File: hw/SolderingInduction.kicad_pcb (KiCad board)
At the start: 4 copper layers, 68.9 x 37.6 mm, 55 parts, among them J1 C116159, J3 RBP_GPIO_CONN, SW1 SW_Push, SW2 SW_Push, SW3 SW_Push, SW4 SW_Push, SW5 SW_Push, SW6 SW_Push, SW7 SW_Push, SW8 SW_Push, U1 ASM1117-3.3, U3 WQ25JVS, U4 RP2040, Y1 X322512MMB4SI

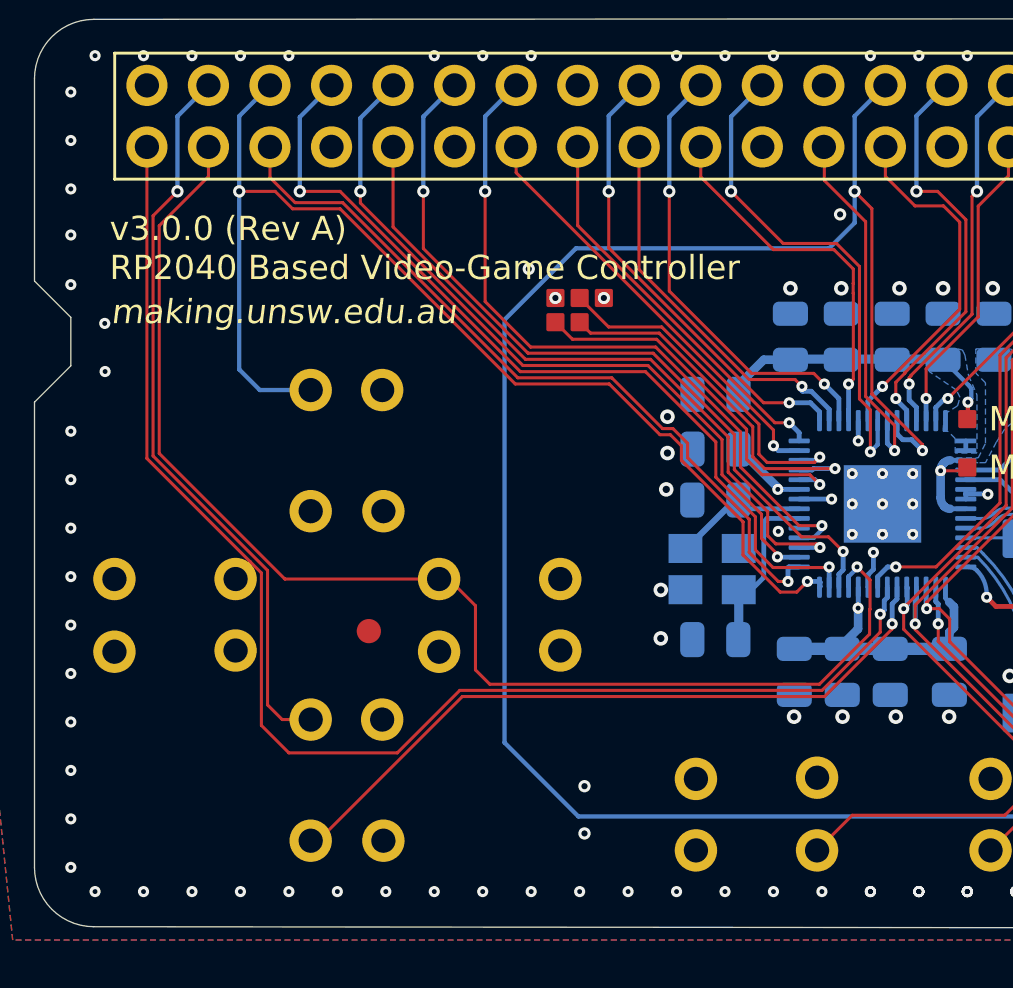
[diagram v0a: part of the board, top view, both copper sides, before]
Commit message: Merge conflict, resolved w/ fw
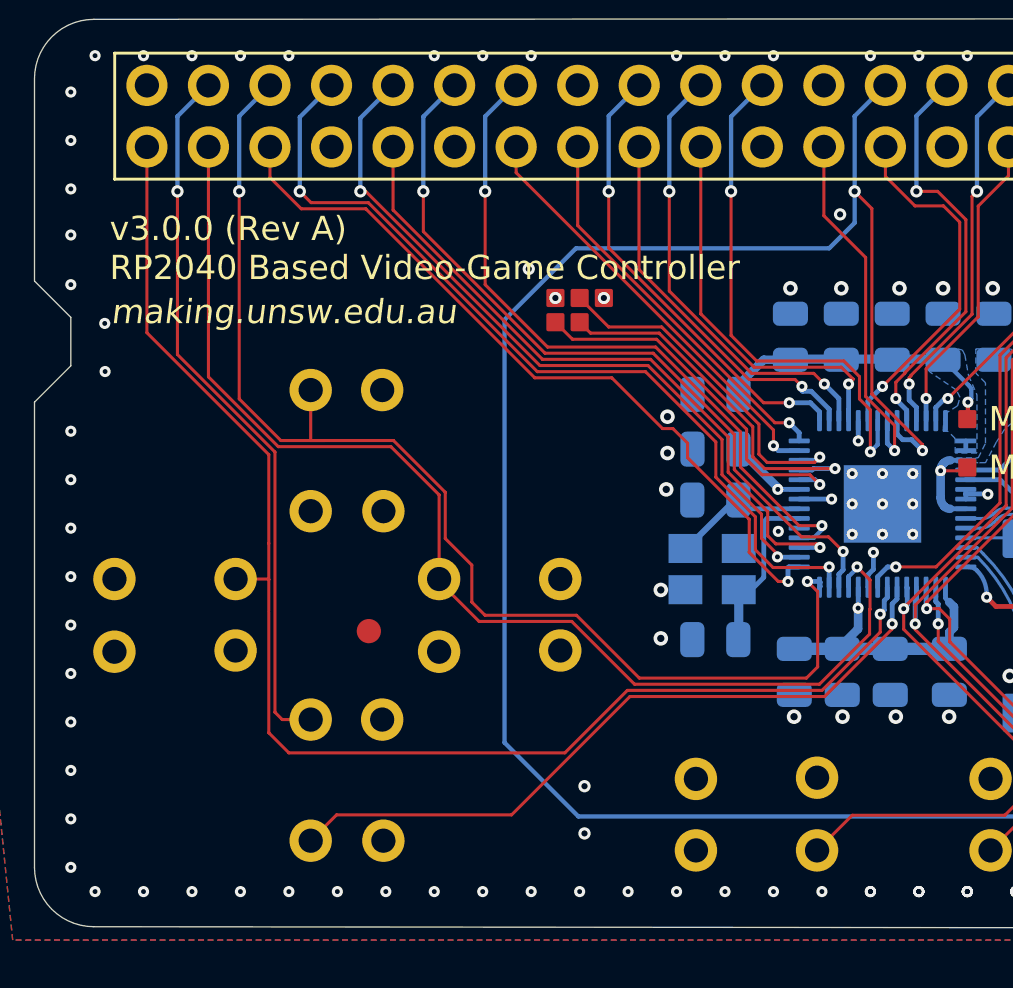
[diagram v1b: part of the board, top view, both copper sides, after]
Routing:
- net /$.GPIO8: track 53.5 -> 49.3 mm
- net /$.GPIO11: track 47.9 -> 51.4 mm
- net /$.GPIO4: track 59.9 -> 59.1 mm
- net /$.GPIO23: track 20.7 -> 21.6 mm
- net /$.GPIO21: track 15.5 -> 16.1 mm

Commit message: Repo cleanup
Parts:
- moved R5 0.56 mm to (148.9, 64.2)
- moved R1 0.17 mm to (154.3, 64.2)
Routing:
- net /USB_VBUS: track 13.1 -> 17.3 mm
- net /$.GPIO5: track 57.3 -> 59.9 mm
- net /$.GPIO11: track 51.4 -> 49.3 mm
- net /$.GPIO8: track 49.3 -> 48.0 mm
- net /$.GPIO10: track 35.7 -> 34.8 mm
- net /$.GPIO9: track 31.8 -> 30.9 mm
- net /$.GPIO14: track 28.3 -> 27.4 mm
- net /$.GPIO15: track 28.9 -> 28.0 mm
- net /$.GPIO13: track 30.8 -> 29.9 mm
- net GND: vias 145 -> 146

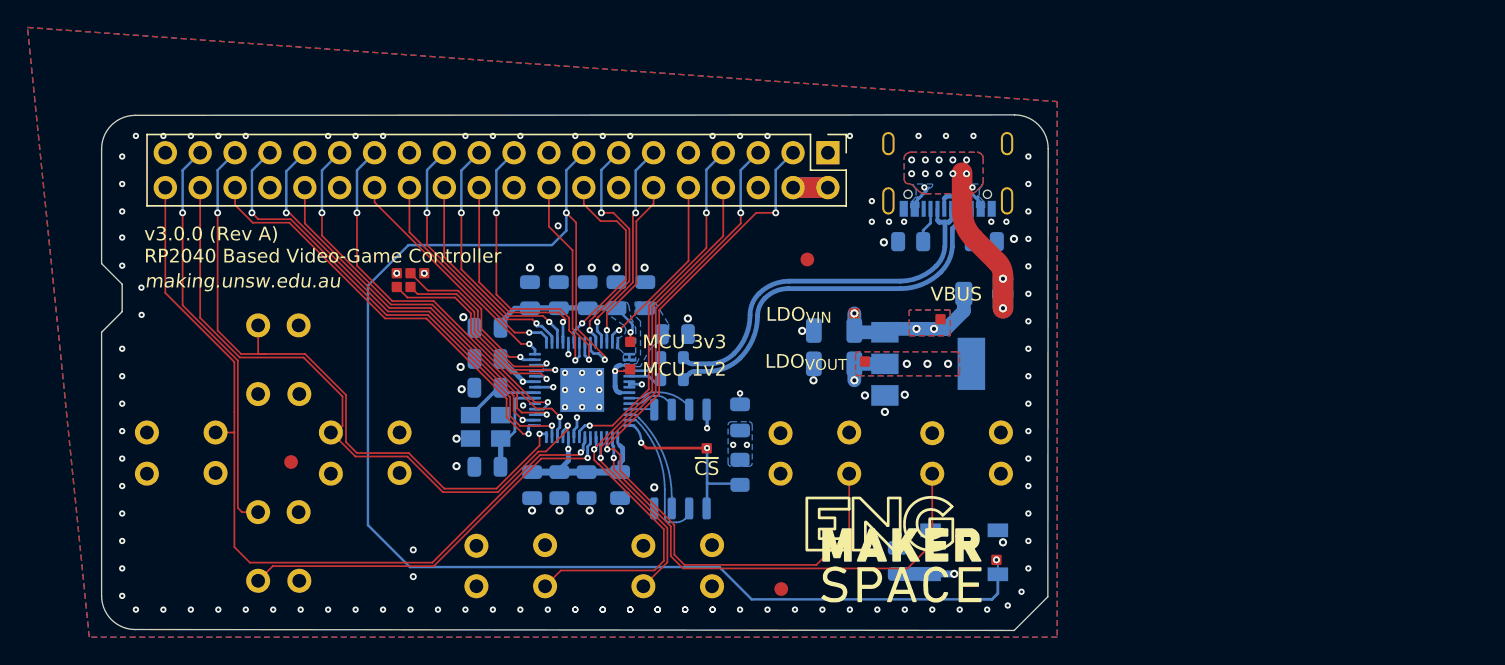
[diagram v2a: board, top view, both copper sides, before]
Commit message: v4.0.0 hw version begins here. Cleaning pinmaps, LED line, power layout, USB layout
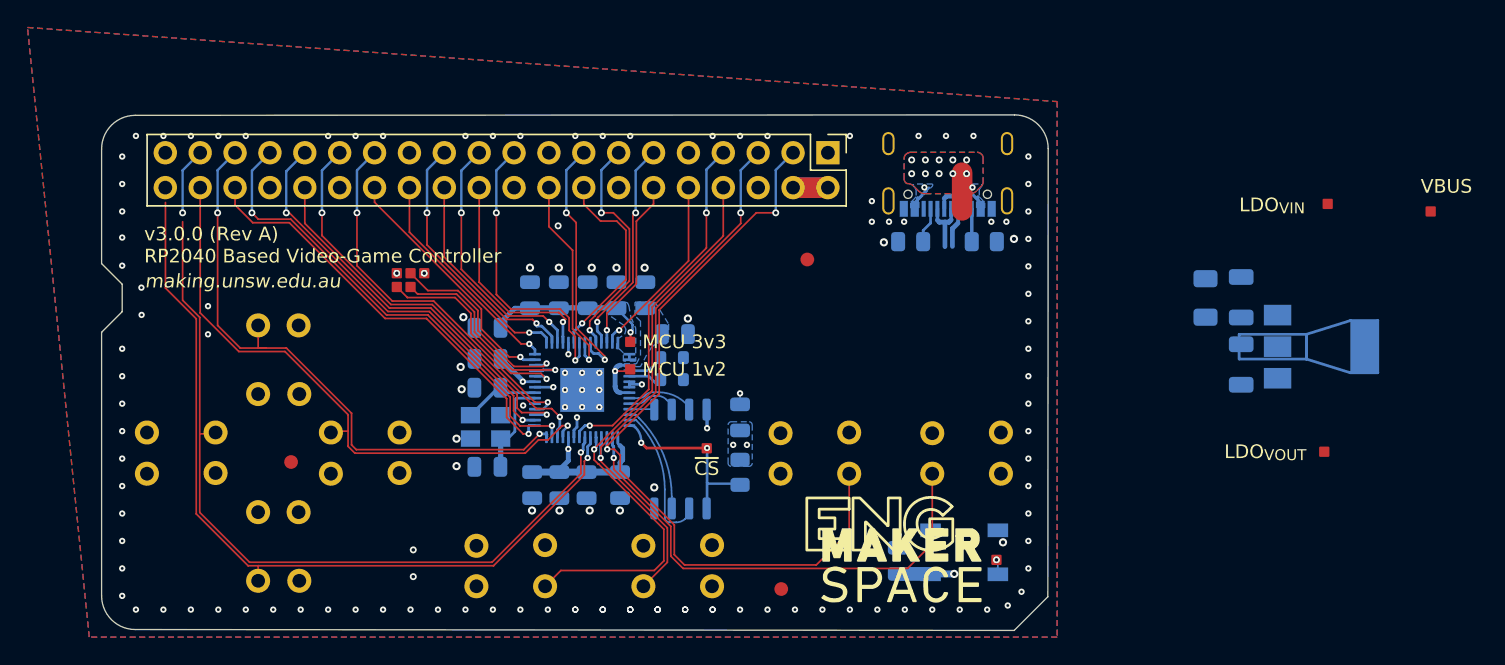
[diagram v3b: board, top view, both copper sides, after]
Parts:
- moved TP8 36.6 mm to (186.8, 62.0)
- moved TP10 35.4 mm to (179.3, 61.5)
- moved TP9 34.1 mm to (179.1, 79.5)
- moved C2 29.7 mm to (173.0, 68.2), turned to 90 degrees
- moved C3 29.7 mm to (173.0, 73.2), turned to -90 degrees
- moved U1 28.6 mm to (178.8, 71.8)
- moved F1 16.2 mm to (170.4, 68.3), turned to -90 degrees
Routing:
- net /$.GPIO25: track 104.3 -> 19.7 mm
- net VBUS: track 55.0 -> 9.24 mm, vias 4 -> 1
- net /USB_{DATA}+: track 30.3 -> 5.56 mm
- net /USB_{DATA}-: track 28.4 -> 4.55 mm
- net /USB_VBUS: track 17.3 -> 7.00 mm, vias 14 -> 12
- net /$.GPIO4: track 59.0 -> 65.1 mm
- net /$.GPIO11: track 49.3 -> 45.1 mm
- net +3V3: track 39.6 -> 36.2 mm, vias 13 -> 9
- net /$.GPIO8: track 48.0 -> 44.9 mm
- net /$.GPIO5: track 59.9 -> 57.7 mm
- net GND: vias 146 -> 143
- removed copper zone on F.Cu, net +3V3
- removed copper zone on B.Cu, net VBUS
- removed copper zone on F.Cu, net VBUS
- removed copper zone on In1.Cu, net VBUS
